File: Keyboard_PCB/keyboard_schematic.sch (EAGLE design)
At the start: 260 parts, among them M1 KEYSWITCH-RGBSMDLED-MX-1U-SMD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, Y2 CRYSTAL-GROUNDEDSMD-3.2X2.5

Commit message: Fixed Keys and added boardpng
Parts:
- removed M1: KEYSWITCH-RGBSMDLED-MX-1U-SMDRGB, Keyboard:KEYSWITCH-RGBSMDLED-MX-1U-SMDRGB
- removed SHIFT1: KEYSWITCH-RGBSMDLED-ALPSMX-2U-SMDRGB, Keyboard:KEYSWITCH-RGBSMDLED-ALPSMX-2U-SMDRGB
- added CTRL1, M2: KEYSWITCH-RGBSMDLED-ALPSMX-1U-SMDRGB, Keyboard:KEYSWITCH-RGBSMDLED-ALPSMX-1U-SMDRGB
- renumbered CAPSLOCK1 to M3, ESC1 to M6, GRAVE1 to M5, TAB1 to M4
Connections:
- new net N$126: DM2.A, M2.P1
- net COL1: now also CTRL1.P0, M2.P0; no longer M1.P0, SHIFT1.P0
- net N$130: now also CTRL1.P1, DM1.A; no longer DM2.A, SHIFT1.P1
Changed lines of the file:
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@@
 <part name="DM1" library="Components" deviceset="DIODE" device="-SOD-123"/>
 <part name="DLOCK" library="Components" deviceset="DIODE" device="-SOD-123"/>
-<part name="M1" library="Keyboard" deviceset="KEYSWITCH-RGBSMDLED" device="-MX-1U-SMDRGB"/>
 <part name="LOCK" library="Keyboard" deviceset="KEYSWITCH-RGBSMDLED" device="-ALPSMX-1U-SMDRGB"/>
 <part name="RANDSONG" library="Keyboard" deviceset="KEYSWITCH-RGBSMDLED" device="-ALPSMX-1U-SMDRGB"/>
 <part name="DNEXTSONG1" library="Components" deviceset="DIODE" device="-SOD-123"/>
 <part name="Y2" library="SparkFun-Clocks" library_urn="urn:adsk.eagle:library:511" deviceset="CRYSTAL-GROUNDED" device="SMD-3.2X2.5" package3d_urn="urn:adsk.eagle:package:37521/1"/>
-<part name="ESC1" library="Keyboard" deviceset="KEYSWITCH-RGBSMDLED" device="-ALPSMX-1U-SMDRGB"/>
-<part name="GRAVE1" library="Keyboard" deviceset="KEYSWITCH-RGBSMDLED" device="-ALPSMX-1U-SMDRGB"/>
-<part name="TAB1" library="Keyboard" deviceset="KEYSWITCH-RGBSMDLED" device="-ALPSMX-1U-SMDRGB"/>
-<part name="CAPSLOCK1" library="Keyboard" deviceset="KEYSWITCH-RGBSMDLED" device="-ALPSMX-1U-SMDRGB"/>
-<part name="SHIFT1" library="Keyboard" deviceset="KEYSWITCH-RGBSMDLED" device="-ALPSMX-2U-SMDRGB"/>
+<part name="M6" library="Keyboard" deviceset="KEYSWITCH-RGBSMDLED" device="-ALPSMX-1U-SMDRGB"/>
+<part name="M5" library="Keyboard" deviceset="KEYSWITCH-RGBSMDLED" device="-ALPSMX-1U-SMDRGB"/>
+<part name="M4" library="Keyboard" deviceset="KEYSWITCH-RGBSMDLED" device="-ALPSMX-1U-SMDRGB"/>
+<part name="M3" library="Keyboard" deviceset="KEYSWITCH-RGBSMDLED" device="-ALPSMX-1U-SMDRGB"/>
+<part name="M2" library="Keyboard" deviceset="KEYSWITCH-RGBSMDLED" device="-ALPSMX-1U-SMDRGB"/>
+<part name="CTRL1" library="Keyboard" deviceset="KEYSWITCH-RGBSMDLED" device="-ALPSMX-1U-SMDRGB"/>
 </parts>
 <sheets>
@@
 <attribute name="VALUE" x="18.9738" y="-254.0254" size="1.778" layer="96" rot="R90"/>
 </instance>
-<instance part="DM1" gate="D$1" x="14.478" y="-322.834" smashed="yes" rot="R90">
-<attribute name="NAME" x="11.8364" y="-325.1454" size="1.778" layer="95" rot="R90"/>
-<attribute name="VALUE" x="18.9738" y="-325.3994" size="1.778" layer="96" rot="R90"/>
+<instance part="DM1" gate="D$1" x="14.478" y="-322.58" smashed="yes" rot="R90">
+<attribute name="NAME" x="11.8364" y="-324.8914" size="1.778" layer="95" rot="R90"/>
+<attribute name="VALUE" x="18.9738" y="-325.1454" size="1.778" layer="96" rot="R90"/>
 </instance>
 <instance part="DLOCK" gate="D$1" x="966.47" y="15.24" smashed="yes" rot="R90">
@@
 <attribute name="VALUE" x="970.9658" y="12.6746" size="1.778" layer="96" rot="R90"/>
 </instance>
-<instance part="M1" gate="G$1" x="11.938" y="-337.82" smashed="yes">
-<attribute name="NAME" x="5.128" y="-332.502" size="1" layer="95"/>
-</instance>
 <instance part="LOCK" gate="G$1" x="963.93" y="0" smashed="yes">
 <attribute name="NAME" x="957.12" y="5.318" size="1" layer="95"/>
@@
 <attribute name="NAME" x="275.59" y="107.696" size="1.778" layer="95" font="vector" align="top-right"/>
 </instance>
-<instance part="ESC1" gate="G$1" x="11.938" y="0" smashed="yes">
+<instance part="M6" gate="G$1" x="11.938" y="0" smashed="yes">
 <attribute name="NAME" x="5.128" y="5.318" size="1" layer="95"/>
 </instance>
-<instance part="GRAVE1" gate="G$1" x="11.938" y="-66.04" smashed="yes">
+<instance part="M5" gate="G$1" x="11.938" y="-66.04" smashed="yes">
 <attribute name="NAME" x="5.128" y="-60.722" size="1" layer="95"/>
 </instance>
-<instance part="TAB1" gate="G$1" x="11.938" y="-134.62" smashed="yes">
+<instance part="M4" gate="G$1" x="11.938" y="-134.62" smashed="yes">
 <attribute name="NAME" x="5.128" y="-129.302" size="1" layer="95"/>
 </instance>
-<instance part="CAPSLOCK1" gate="G$1" x="11.938" y="-195.58" smashed="yes">
+<instance part="M3" gate="G$1" x="11.938" y="-195.58" smashed="yes">
 <attribute name="NAME" x="5.128" y="-190.262" size="1" layer="95"/>
 </instance>
-<instance part="SHIFT1" gate="G$1" x="11.938" y="-266.7" smashed="yes">
+<instance part="M2" gate="G$1" x="11.938" y="-266.7" smashed="yes">
 <attribute name="NAME" x="5.128" y="-261.382" size="1" layer="95"/>
 </instance>
+<instance part="CTRL1" gate="G$1" x="11.938" y="-337.82" smashed="yes">
+<attribute name="NAME" x="5.128" y="-332.502" size="1" layer="95"/>
+</instance>
 </instances>
 <busses>
@@
 <bus name="ROW4:ROW4.1,ROW4.2">
 <segment>
-<wire x1="17.78" y1="-170.18" x2="967.74" y2="-170.18" width="0.762" layer="92"/>
+<wire x1="15.24" y1="-170.18" x2="967.74" y2="-170.18" width="0.762" layer="92"/>
 </segment>
 </bus>
 <bus name="ROW5:ROW5.1,ROW5.2">
 <segment>
-<wire x1="20.32" y1="-241.3" x2="967.74" y2="-241.3" width="0.762" layer="92"/>
+<wire x1="17.78" y1="-241.3" x2="965.2" y2="-241.3" width="0.762" layer="92"/>
 </segment>
 </bus>
@@
 <segment>
 <pinref part="DM1" gate="D$1" pin="C"/>
-<wire x1="14.478" y1="-317.754" x2="14.478" y2="-313.182" width="0.1524" layer="91"/>
+<wire x1="14.478" y1="-317.5" x2="14.478" y2="-313.182" width="0.1524" layer="91"/>
 <wire x1="14.478" y1="-313.182" x2="15.24" y2="-312.42" width="0.1524" layer="91"/>
 </segment>
@@
 <junction x="33.02" y="-33.02"/>
 <wire x1="1.778" y1="2.54" x2="0" y2="0" width="0.1524" layer="91"/>
-<pinref part="M1" gate="G$1" pin="P0"/>
 <wire x1="0" y1="-33.02" x2="0" y2="-63.5" width="0.1524" layer="91"/>
 <wire x1="0" y1="-63.5" x2="0" y2="-132.08" width="0.1524" layer="91"/>
@@
 <wire x1="0" y1="-335.28" x2="1.778" y2="-335.28" width="0.1524" layer="91"/>
 <junction x="0" y="-33.02"/>
-<pinref part="ESC1" gate="G$1" pin="P0"/>
-<pinref part="GRAVE1" gate="G$1" pin="P0"/>
+<pinref part="M6" gate="G$1" pin="P0"/>
+<pinref part="M5" gate="G$1" pin="P0"/>
 <wire x1="1.778" y1="-63.5" x2="0" y2="-63.5" width="0.1524" layer="91"/>
 <junction x="0" y="-63.5"/>
-<pinref part="TAB1" gate="G$1" pin="P0"/>
+<pinref part="M4" gate="G$1" pin="P0"/>
 <wire x1="1.778" y1="-132.08" x2="0" y2="-132.08" width="0.1524" layer="91"/>
 <junction x="0" y="-132.08"/>
-<pinref part="CAPSLOCK1" gate="G$1" pin="P0"/>
+<pinref part="M3" gate="G$1" pin="P0"/>
 <wire x1="1.778" y1="-193.04" x2="0" y2="-193.04" width="0.1524" layer="91"/>
 <junction x="0" y="-193.04"/>
-<pinref part="SHIFT1" gate="G$1" pin="P0"/>
 <wire x1="1.778" y1="-264.16" x2="0" y2="-264.16" width="0.1524" layer="91"/>
 <junction x="0" y="-264.16"/>
@@
 <junction x="0" y="0"/>
 <label x="0" y="40.64" size="1.778" layer="95" rot="R90"/>
+<pinref part="M2" gate="G$1" pin="P0"/>
+<pinref part="CTRL1" gate="G$1" pin="P0"/>
 </segment>
 <segment>
@@
 <net name="N$120" class="0">
 <segment>
-<pinref part="ESC1" gate="G$1" pin="P1"/>
+<pinref part="M6" gate="G$1" pin="P1"/>
 <pinref part="DM6" gate="D$1" pin="A"/>
 </segment>
@@
 <net name="N$127" class="0">
 <segment>
-<pinref part="GRAVE1" gate="G$1" pin="P1"/>
+<pinref part="M5" gate="G$1" pin="P1"/>
 <pinref part="DM5" gate="D$1" pin="A"/>
 </segment>
@@
 <net name="N$128" class="0">
 <segment>
-<pinref part="TAB1" gate="G$1" pin="P1"/>
+<pinref part="M4" gate="G$1" pin="P1"/>
 <pinref part="DM4" gate="D$1" pin="A"/>
 </segment>
@@
 <net name="N$129" class="0">
 <segment>
-<pinref part="CAPSLOCK1" gate="G$1" pin="P1"/>
+<pinref part="M3" gate="G$1" pin="P1"/>
 <pinref part="DM3" gate="D$1" pin="A"/>
 </segment>
 </net>
-<net name="N$130" class="0">
-<segment>
-<pinref part="SHIFT1" gate="G$1" pin="P1"/>
-<pinref part="DM2" gate="D$1" pin="A"/>
-</segment>
-</net>
 <net name="COL2" class="0">
 <segment>
@@
 </segment>
 </net>
+<net name="N$126" class="0">
+<segment>
+<pinref part="M2" gate="G$1" pin="P1"/>
+<pinref part="DM2" gate="D$1" pin="A"/>
+</segment>
+</net>
+<net name="N$130" class="0">
+<segment>
+<pinref part="CTRL1" gate="G$1" pin="P1"/>
+<pinref part="DM1" gate="D$1" pin="A"/>
+</segment>
+</net>

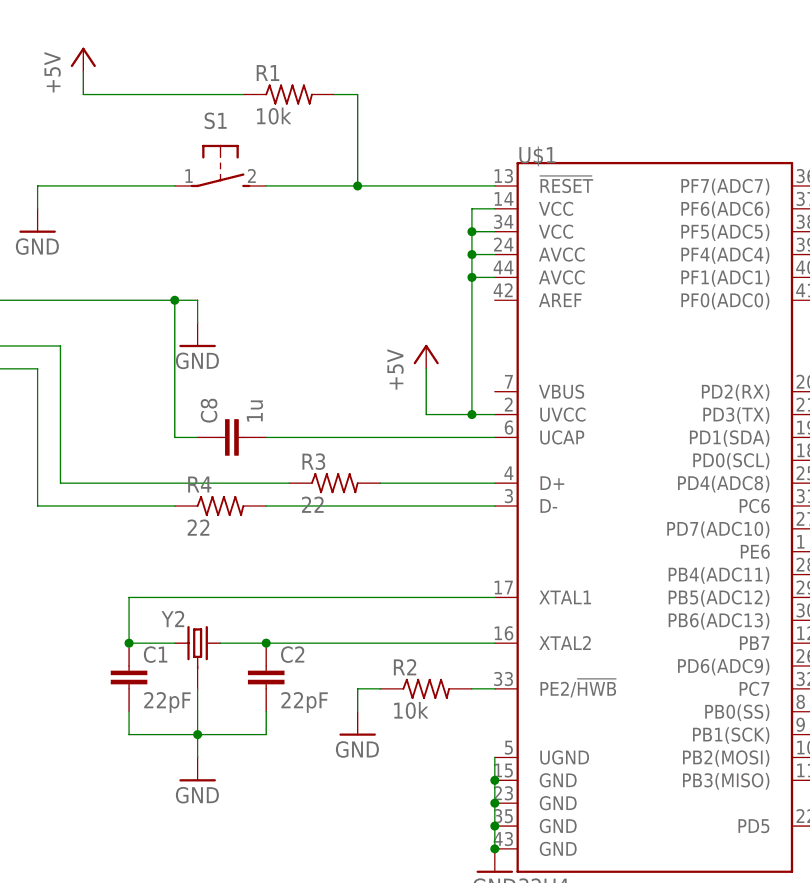
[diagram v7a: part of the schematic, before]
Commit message: Updated Schematic Names
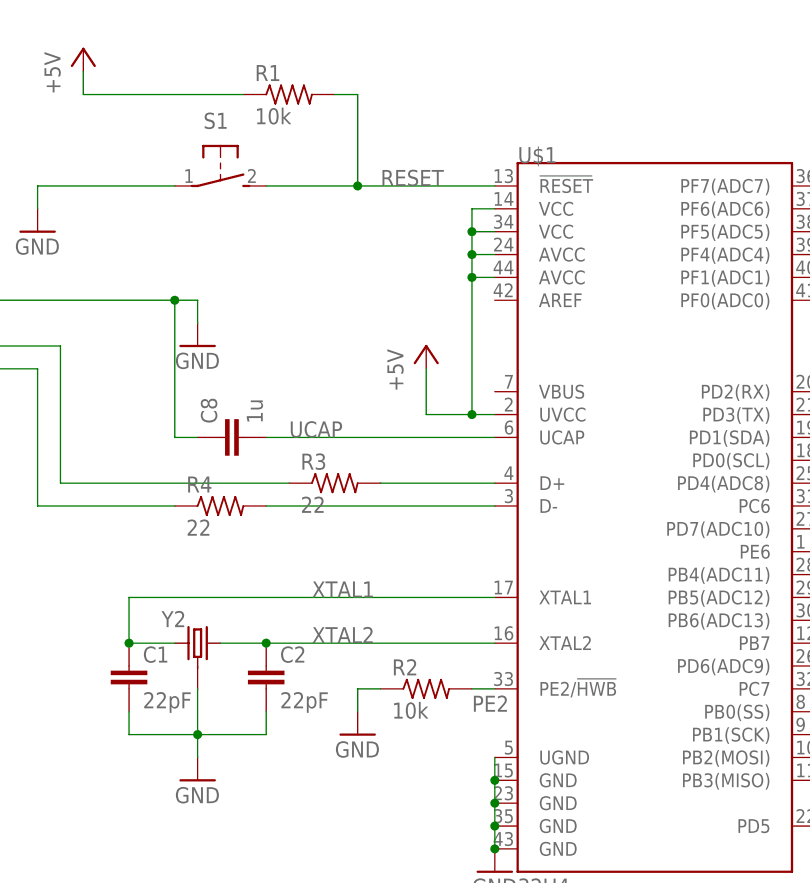
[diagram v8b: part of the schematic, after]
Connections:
- net N$116 renamed XTAL1
- net N$117 renamed XTAL2
- net N$118 renamed RESET
- net N$119 renamed PE2
- net N$121 renamed D+USB
- net N$122 renamed D-USB
- net N$123 renamed D+32U
- net N$124 renamed D-32U4
- net N$125 renamed UCAP
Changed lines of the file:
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@@
 </segment>
 </net>
-<net name="N$116" class="0">
+<net name="XTAL1" class="0">
 <segment>
 <pinref part="C1" gate="G$1" pin="1"/>
@@
 <junction x="269.24" y="104.14"/>
 <pinref part="Y2" gate="G$1" pin="1"/>
-</segment>
-</net>
-<net name="N$117" class="0">
+<label x="289.56" y="109.22" size="1.778" layer="95"/>
+</segment>
+</net>
+<net name="XTAL2" class="0">
 <segment>
 <pinref part="C2" gate="G$1" pin="1"/>
@@
 <junction x="284.48" y="104.14"/>
 <pinref part="Y2" gate="G$1" pin="2"/>
+<label x="289.56" y="104.14" size="1.778" layer="95"/>
 </segment>
 </net>
@@
 </segment>
 </net>
-<net name="N$118" class="0">
+<net name="RESET" class="0">
 <segment>
 <pinref part="S1" gate="1" pin="S"/>
@@
 <wire x1="294.64" y1="165.1" x2="294.64" y2="154.94" width="0.1524" layer="91"/>
 <junction x="294.64" y="154.94"/>
-</segment>
-</net>
-<net name="N$119" class="0">
+<label x="297.18" y="154.94" size="1.778" layer="95"/>
+</segment>
+</net>
+<net name="PE2" class="0">
 <segment>
 <pinref part="R2" gate="G$1" pin="2"/>
 <pinref part="U$1" gate="G$1" pin="PE2/!HWB"/>
 <wire x1="307.34" y1="99.06" x2="309.88" y2="99.06" width="0.1524" layer="91"/>
-</segment>
-</net>
-<net name="N$121" class="0">
+<label x="307.34" y="96.52" size="1.778" layer="95"/>
+</segment>
+</net>
+<net name="D+USB" class="0">
 <segment>
 <pinref part="J1" gate="G$1" pin="D+"/>
@@
 </segment>
 </net>
-<net name="N$122" class="0">
+<net name="D-USB" class="0">
 <segment>
 <pinref part="J1" gate="G$1" pin="D-"/>
@@
 </segment>
 </net>
-<net name="N$123" class="0">
+<net name="D+32U" class="0">
 <segment>
 <pinref part="R3" gate="G$1" pin="2"/>
@@
 </segment>
 </net>
-<net name="N$124" class="0">
+<net name="D-32U4" class="0">
 <segment>
 <pinref part="U$1" gate="G$1" pin="D-"/>
@@
 </segment>
 </net>
-<net name="N$125" class="0">
+<net name="UCAP" class="0">
 <segment>
 <pinref part="C8" gate="G$1" pin="2"/>
 <pinref part="U$1" gate="G$1" pin="UCAP"/>
 <wire x1="284.48" y1="127" x2="309.88" y2="127" width="0.1524" layer="91"/>
-</segment>
-</net>
+<label x="287.02" y="127" size="1.778" layer="95"/>
+</segment>
+</net>
